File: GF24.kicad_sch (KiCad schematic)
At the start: 11 parts, among them SW1 RST, U1 STM32F031C4T6, U2 MAX-M10S, Y1 Crystal

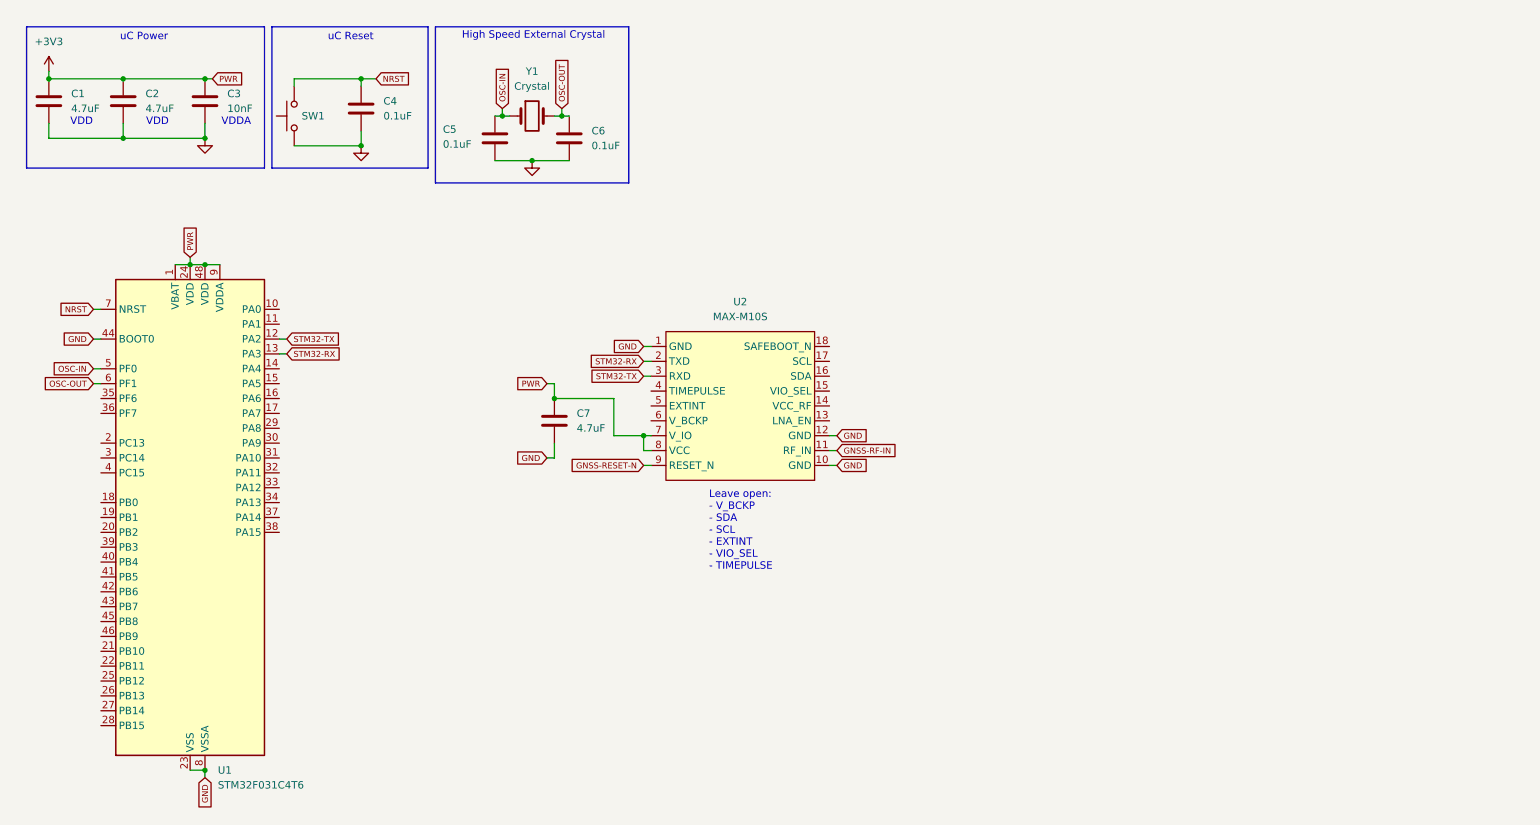
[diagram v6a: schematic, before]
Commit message: added boot mode and battery
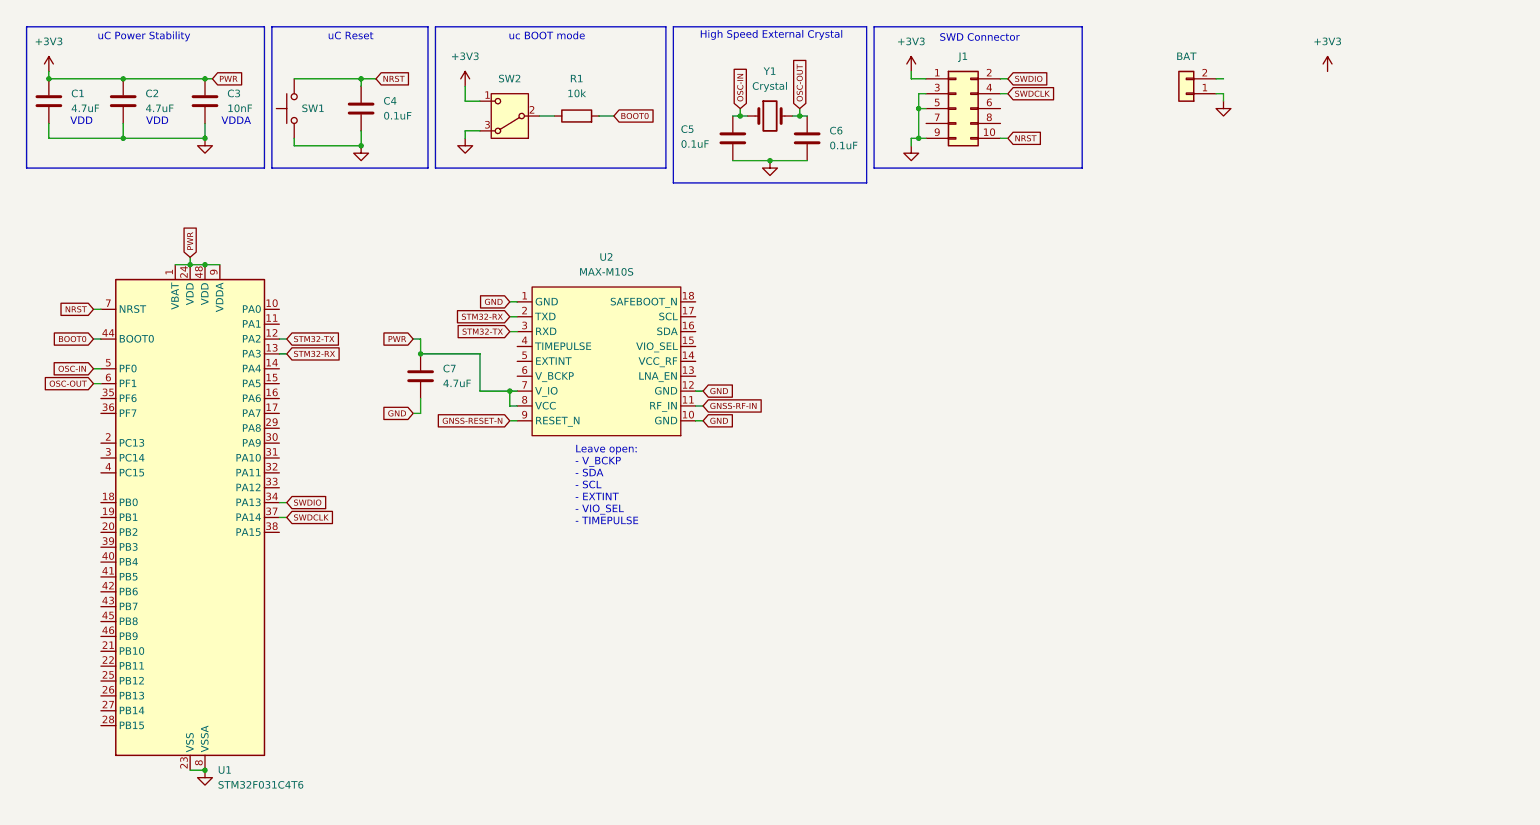
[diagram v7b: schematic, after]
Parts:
- added BAT: Conn_01x02, symbol Connector_Generic:Conn_01x02
- added J1: Conn_02x05_Odd_Even, symbol Connector_Generic:Conn_02x05_Odd_Even
- added R1: 10k, symbol Device:R
- added SW2: SW_Nidec_CAS-120A1, Button_Switch_SMD:Nidec_Copal_CAS-120A, symbol Switch:SW_Nidec_CAS-120A1
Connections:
- net +3V3: now also J1.1 (Pin_1), SW2.1 (C)
- net GND: now also BAT.1 (Pin_1), J1.3 (Pin_3), J1.5 (Pin_5), J1.9 (Pin_9), SW2.3 (A); no longer U1.44 (BOOT0)
- net NRST: now also J1.10 (Pin_10)
- net SWDIO: now reaches U1.34 (PA13)
- net SWDIO: now also J1.2 (Pin_2)
- net SWDCLK: now reaches U1.37 (PA14)
- net SWDCLK: now also J1.4 (Pin_4)
- new net: R1.1, SW2.2 (B)
- new net BOOT0: R1.2, U1.44 (BOOT0)
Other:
- note added: "SWD Connector"
- note added: "uC Power Stability"
- note added: "uc BOOT mode"
- note removed: "uC Power"
- moved on the sheet: C5, C6, C7, SW1, U2, Y1

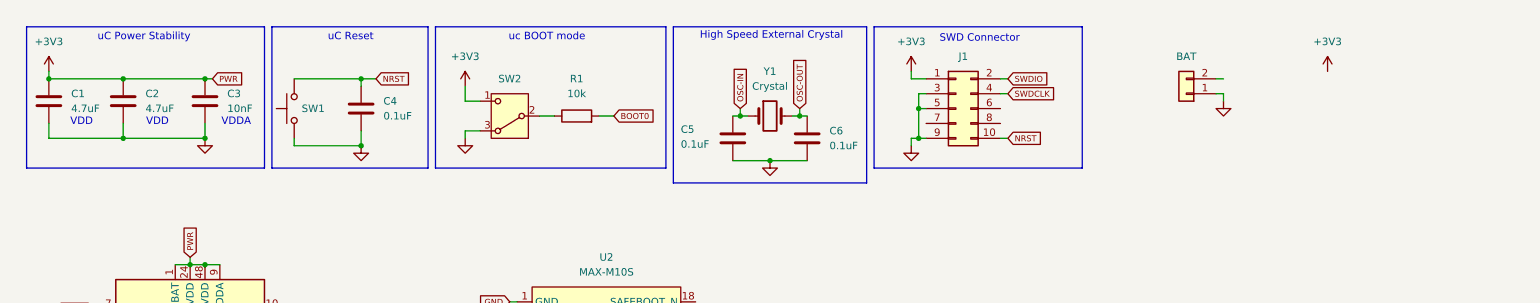
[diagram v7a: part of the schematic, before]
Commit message: added voltage regulator
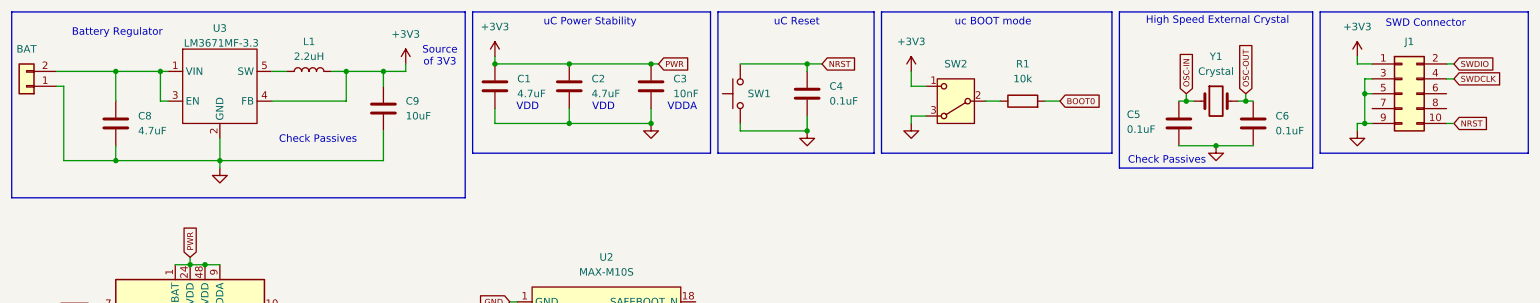
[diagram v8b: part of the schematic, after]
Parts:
- added C8: 4.7uF, Capacitor_SMD:C_1210_3225Metric_Pad1.33x2.70mm_HandSolder, symbol Device:C
- added C9: 10uF, Capacitor_SMD:C_1210_3225Metric_Pad1.33x2.70mm_HandSolder, symbol Device:C
- added L1: 2.2uH, symbol Device:L
- added U3: LM3671MF-3.3, symbol MB-V-REG:LM3671
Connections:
- net +3V3: now also C9.1, L1.2, U3.4 (FB)
- net GND: now also C8.2, C9.2, U3.2 (GND)
- net at BAT.2 (Pin_2): now also C8.1, U3.1 (VIN), U3.3 (EN)
- new net: L1.1, U3.5 (SW)
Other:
- note added: "Battery Regulator"
- note added: "Check Passives"
- note added: "Source of 3V3"
- moved on the sheet: BAT, C1, C2, C3, C4, C5, C6, J1, R1, SW1, SW2, Y1
